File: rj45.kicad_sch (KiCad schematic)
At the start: 4 parts, among them J4 RJ45-Ethernet

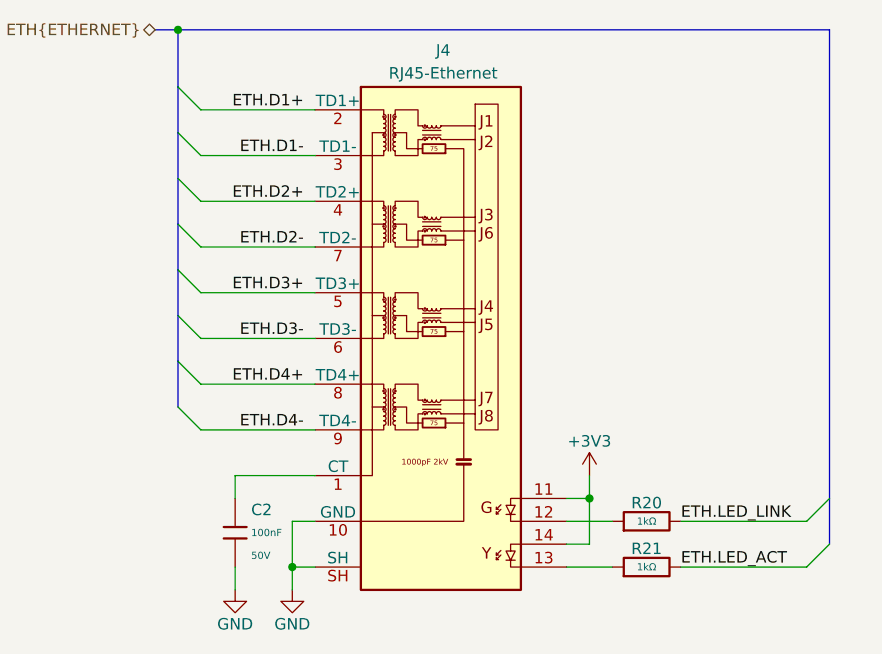
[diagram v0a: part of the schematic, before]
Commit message: [#1] WIP: Change components to ones from the global library, refactor schematic
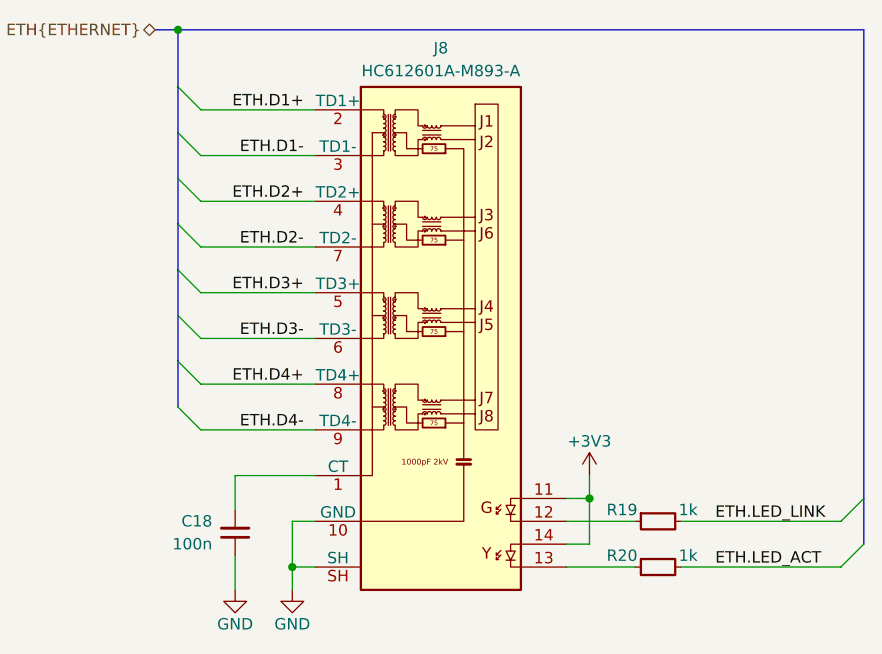
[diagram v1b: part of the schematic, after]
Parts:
- removed C2: 100nF, PCM_JLCPCB:C_0402, symbol PCM_JLCPCB-Capacitors:0402,100nF,(2)
- removed J4: RJ45-Ethernet, lib:RJ45-HC612601A-M893-A, symbol connectors:RJ45-HC612601A-M893-A
- removed R20, R21: 1kΩ, PCM_JLCPCB:R_0402, symbol PCM_JLCPCB-Resistors:0402,1kΩ
- added C18: C-100n-0402, DW-footprints:C_0402_1005Metric, symbol DW-capacitors:C-100n-0402
- added J8: RJ45_HC612601A-M893-A, DW-footprints:RJ45_HC612601A-M893-A, symbol DW-connectors:RJ45_HC612601A-M893-A
- added R19, R20: R-1k-0402, DW-footprints:R_0402_1005Metric, symbol DW-resistors:R-1k-0402
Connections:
- net +3V3: now also J8.11, J8.14
- net ETH.D1+: now also J8.2 (TD1+)
- net ETH.D1-: now also J8.3 (TD1-)
- net ETH.D2+: now also J8.4 (TD2+)
- net ETH.D2-: now also J8.7 (TD2-)
- net ETH.D3+: now also J8.5 (TD3+)
- net ETH.D3-: now also J8.6 (TD3-)
- net ETH.D4+: now also J8.8 (TD4+)
- net ETH.D4-: now also J8.9 (TD4-)
- net ETH.LED_ACT: now also R20.2
- net ETH.LED_LINK: now also R19.2
- net GND: now also C18.1, J8.10 (GND), J8.SH
- new net: J8.13, R20.1
- new net: J8.12, R19.1
- new net: C18.2, J8.1 (CT)

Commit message: [#1] Re-annotate schematic
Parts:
- renumbered C18 to C2, J8 to J6, R19 to R8, R20 to R9
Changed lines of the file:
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@@
 		(on_board yes)
 		(dnp no)
-		(property "Reference" "#PWR21"
+		(property "Reference" "#PWR031"
 			(at 186.69 182.88 0)
 			(effects
@@
 			(project "cm5-module"
 				(path "/090a8e41-87a8-4fb1-998b-60a2c0dc4cee/dd50f821-f925-406c-ae05-a2a500dfc6d6"
-					(reference "#PWR21")
+					(reference "#PWR031")
 					(unit 1)
 				)
@@
 		(on_board yes)
 		(dnp no)
-		(property "Reference" "#PWR013"
+		(property "Reference" "#PWR029"
 			(at 219.71 167.64 0)
 			(effects
@@
 			(project ""
 				(path "/090a8e41-87a8-4fb1-998b-60a2c0dc4cee/dd50f821-f925-406c-ae05-a2a500dfc6d6"
-					(reference "#PWR013")
+					(reference "#PWR029")
 					(unit 1)
 				)
@@
 		(on_board yes)
 		(dnp no)
-		(property "Reference" "R20"
+		(property "Reference" "R9"
 			(at 225.044 172.72 0)
 			(effects
@@
 			(project "cm5-module"
 				(path "/090a8e41-87a8-4fb1-998b-60a2c0dc4cee/dd50f821-f925-406c-ae05-a2a500dfc6d6"
-					(reference "R20")
+					(reference "R9")
 					(unit 1)
 				)
@@
 		(on_board yes)
 		(dnp no)
-		(property "Reference" "R19"
+		(property "Reference" "R8"
 			(at 225.044 167.64 0)
 			(effects
@@
 			(project ""
 				(path "/090a8e41-87a8-4fb1-998b-60a2c0dc4cee/dd50f821-f925-406c-ae05-a2a500dfc6d6"
-					(reference "R19")
+					(reference "R8")
 					(unit 1)
 				)
@@
 		(on_board yes)
 		(dnp no)
-		(property "Reference" "J8"
+		(property "Reference" "J6"
 			(at 203.2 116.332 0)
 			(effects
@@
 			(project ""
 				(path "/090a8e41-87a8-4fb1-998b-60a2c0dc4cee/dd50f821-f925-406c-ae05-a2a500dfc6d6"
-					(reference "J8")
+					(reference "J6")
 					(unit 1)
 				)
@@
 		(on_board yes)
 		(dnp no)
-		(property "Reference" "#PWR20"
+		(property "Reference" "#PWR030"
 			(at 180.34 182.88 0)
 			(effects
@@
 			(project "cm5-module"
 				(path "/090a8e41-87a8-4fb1-998b-60a2c0dc4cee/dd50f821-f925-406c-ae05-a2a500dfc6d6"
-					(reference "#PWR20")
+					(reference "#PWR030")
 					(unit 1)
 				)
@@
 		(on_board yes)
 		(dnp no)
-		(property "Reference" "C18"
+		(property "Reference" "C2"
 			(at 177.8 168.9036 90)
 			(effects
@@
 			(project "cm5-module"
 				(path "/090a8e41-87a8-4fb1-998b-60a2c0dc4cee/dd50f821-f925-406c-ae05-a2a500dfc6d6"
-					(reference "C18")
+					(reference "C2")
 					(unit 1)
 				)

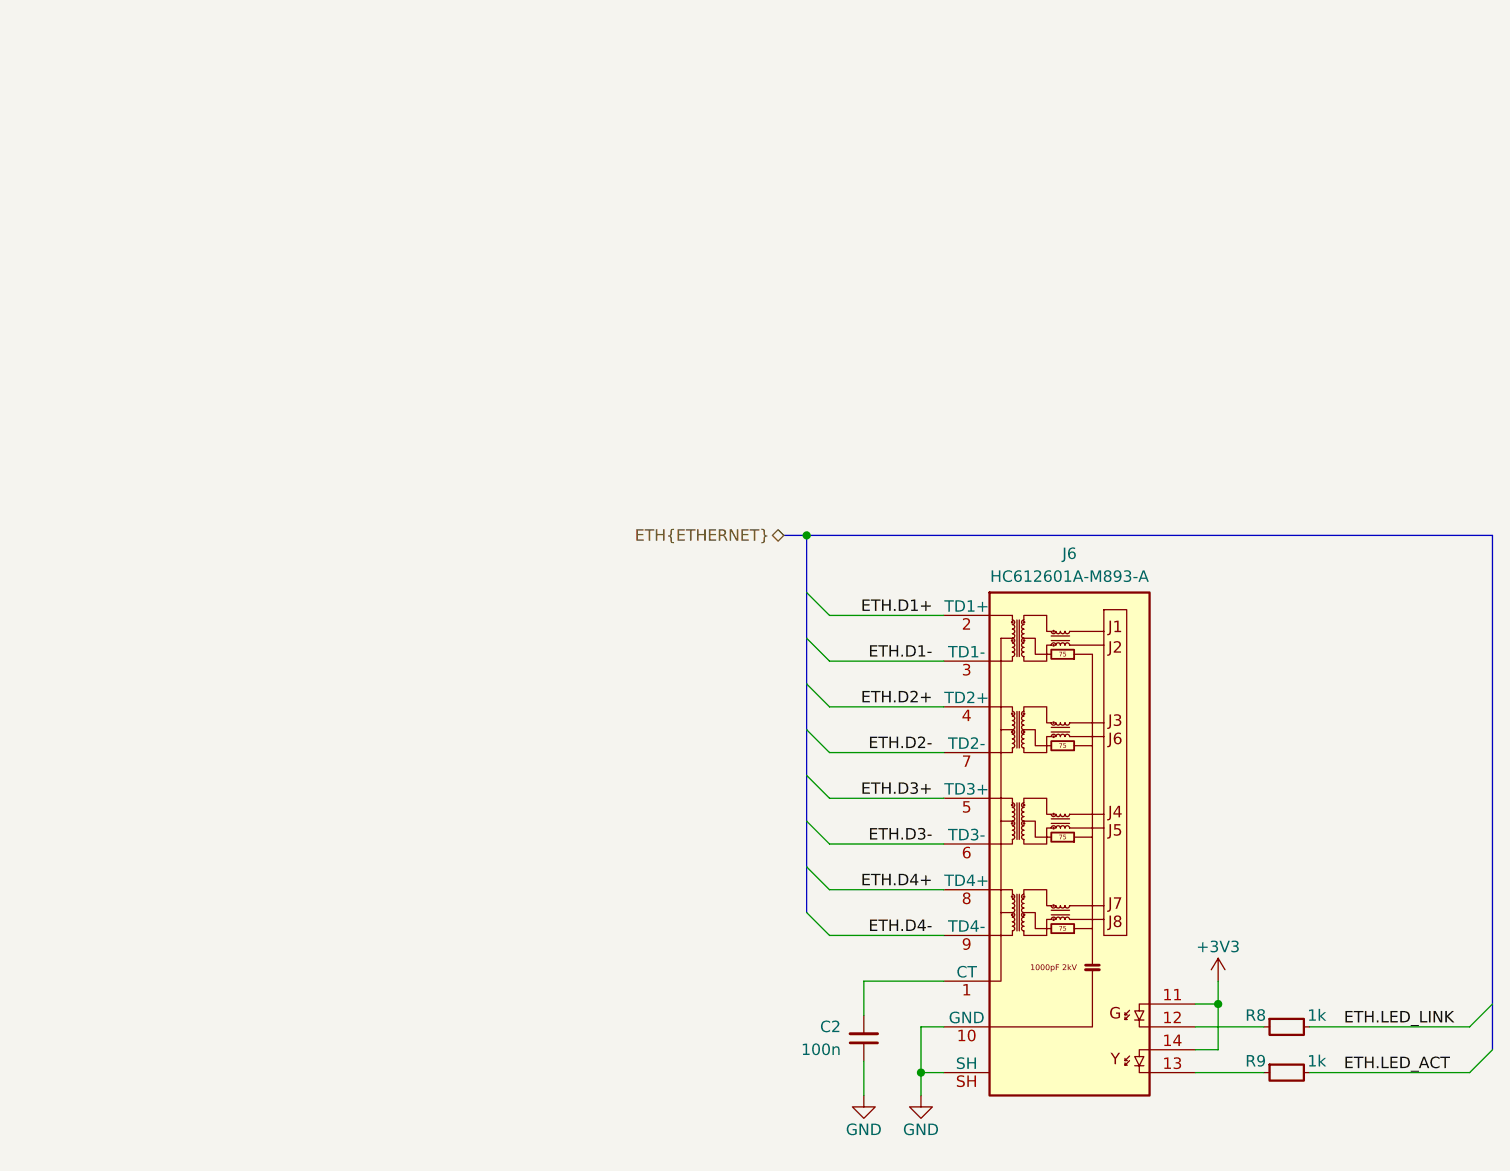
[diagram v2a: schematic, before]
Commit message: [#1] WIP: Refactor schematic
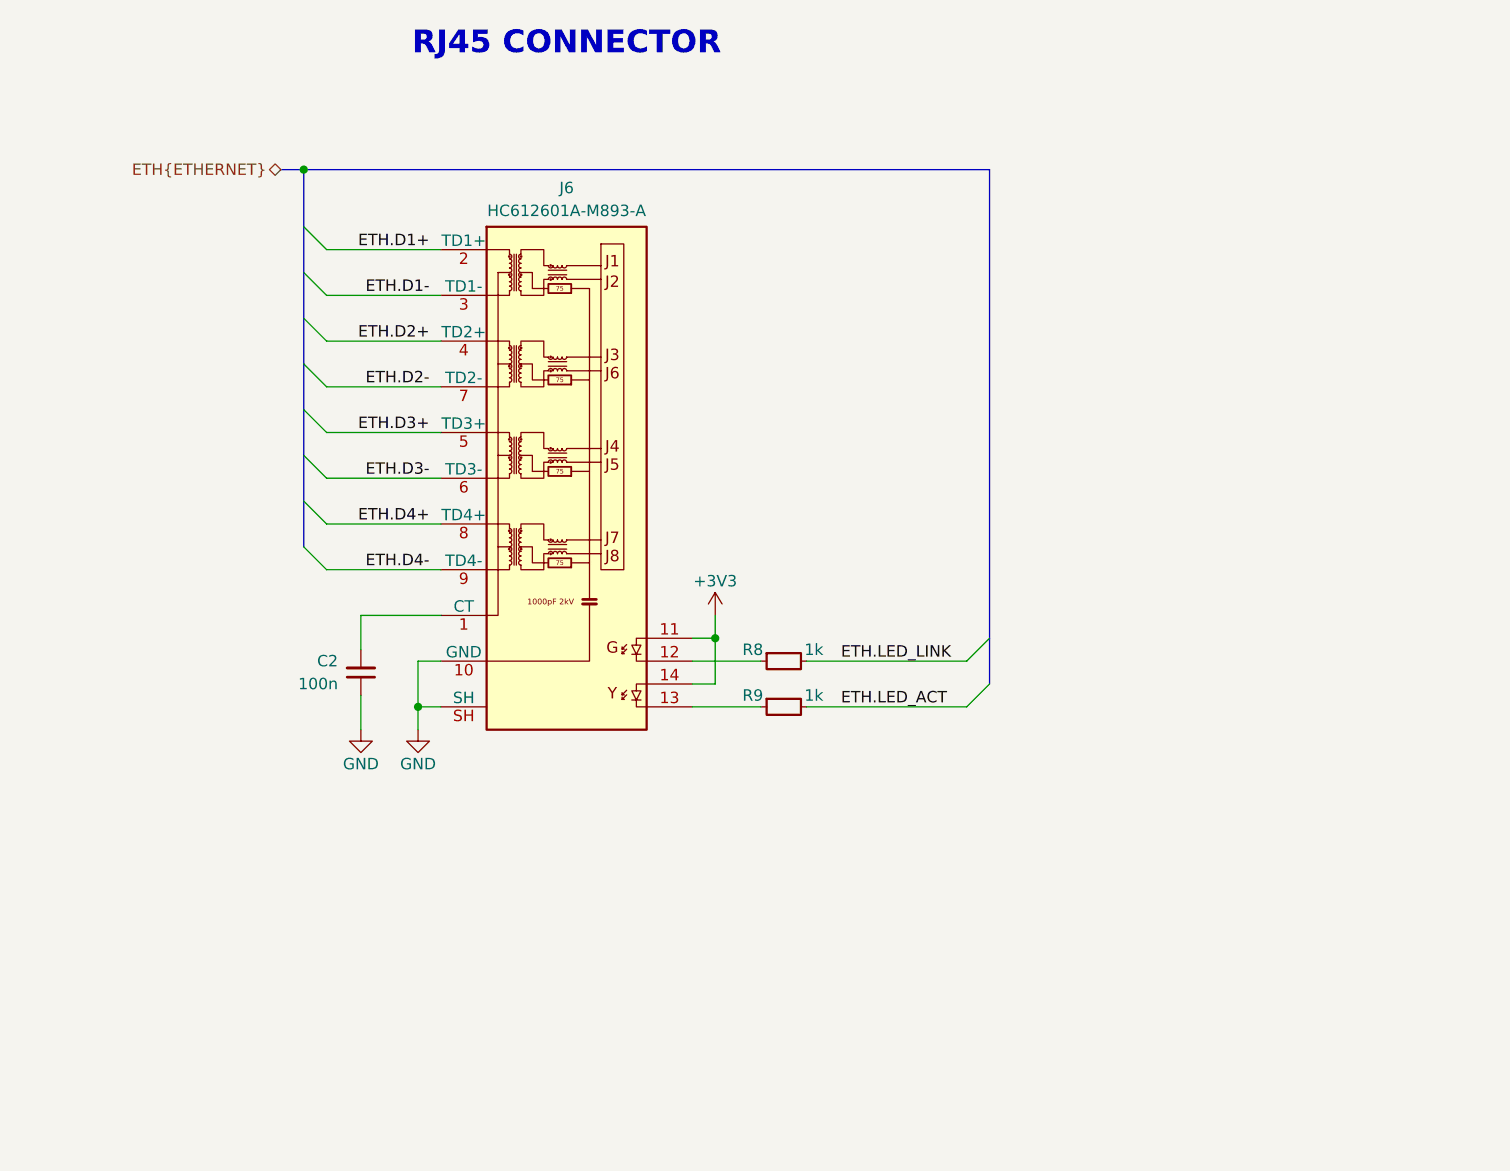
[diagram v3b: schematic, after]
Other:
- note added: "RJ45 CONNECTOR"
- moved on the sheet: C2, J6, R8, R9

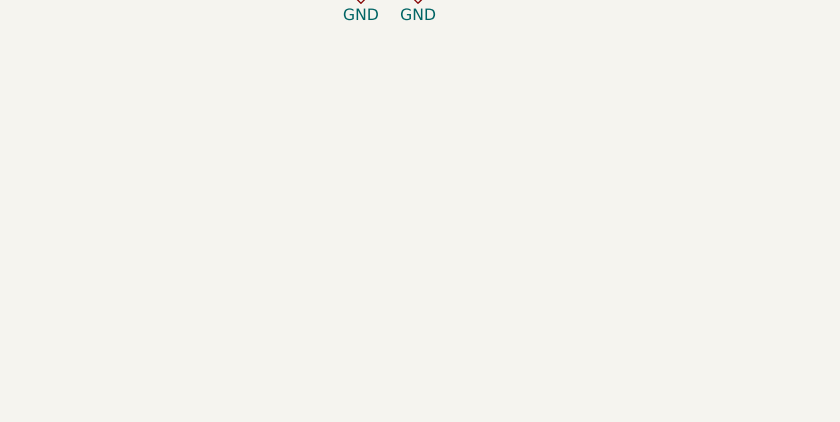
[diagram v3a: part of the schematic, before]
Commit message: [#3] Add TVS, route HDMI and fanout ETH
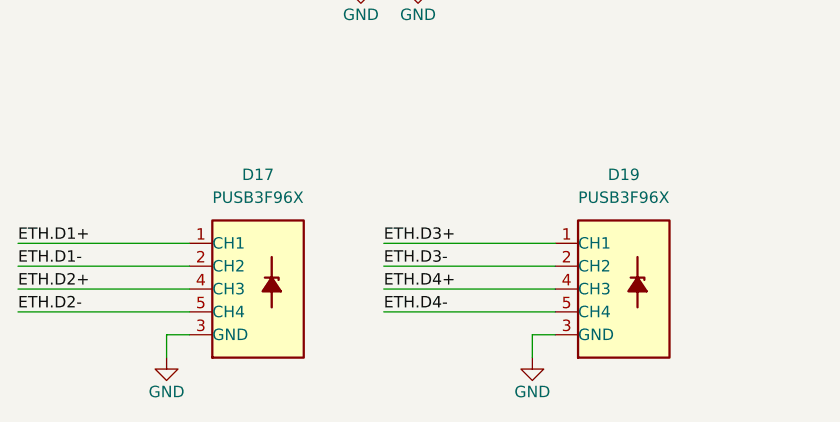
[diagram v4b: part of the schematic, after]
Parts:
- added D17, D19: PUSB3F96X, DW-footprints:SOT1176-1, symbol DW-TVS:PUSB3F96X
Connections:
- net ETH.D1+: now also D17.1 (CH1), D17.10 (CH1)
- net ETH.D1-: now also D17.2 (CH2), D17.9 (CH2)
- net ETH.D2+: now also D17.4 (CH3), D17.7 (CH3)
- net ETH.D2-: now also D17.5 (CH4), D17.6 (CH4)
- net ETH.D3+: now also D19.1 (CH1), D19.10 (CH1)
- net ETH.D3-: now also D19.2 (CH2), D19.9 (CH2)
- net ETH.D4+: now also D19.4 (CH3), D19.7 (CH3)
- net ETH.D4-: now also D19.5 (CH4), D19.6 (CH4)
- net GND: now also D17.3 (GND), D17.8 (GND), D19.3 (GND), D19.8 (GND)
